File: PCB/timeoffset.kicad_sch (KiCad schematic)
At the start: 10 parts, among them J1 Conn_01x03, Q1 IRF7204_jandevalua, U1 ATtiny13A-SU

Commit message: Smaller form
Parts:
- added J2: Conn_01x03, Connector_JST:JST_PH_S3B-PH-K_1x03_P2.00mm_Horizontal, symbol Connector_Generic:Conn_01x03
- D1: footprint Diode_SMD:D_SMB -> Diode_SMD:D_SMA
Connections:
- net at C1.1, C2.1, D1.1 (K)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: now also J2.2 (Pin_2); no longer Q1.1 (S2), R2.2
- net at D1.2 (A), J1.2 (Pin_2), R1.1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: now also J2.1 (Pin_1)
- new net: J2.3 (Pin_3), Q1.1 (S2), R2.2
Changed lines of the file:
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@@
-(kicad_sch (version 20201015) (generator eeschema)
-  (page 1 1)
+(kicad_sch (version 20210621) (generator eeschema)
   (paper "A4")
-  (junction (at 64.77 46.99) (diameter 1.016) (color 0 0 0 0))
+  (junction (at 64.77 40.64) (diameter 1.016) (color 0 0 0 0))
   (junction (at 71.12 52.07) (diameter 1.016) (color 0 0 0 0))
   (junction (at 71.12 87.63) (diameter 1.016) (color 0 0 0 0))
   (junction (at 77.47 52.07) (diameter 1.016) (color 0 0 0 0))
   (junction (at 77.47 87.63) (diameter 1.016) (color 0 0 0 0))
+  (junction (at 88.8615 40.64) (diameter 1.016) (color 0 0 0 0))
   (junction (at 88.9 40.64) (diameter 1.016) (color 0 0 0 0))
   (junction (at 99.06 87.63) (diameter 1.016) (color 0 0 0 0))
-  (junction (at 99.06 91.44) (diameter 1.016) (color 0 0 0 0))
   (junction (at 119.38 60.96) (diameter 1.016) (color 0 0 0 0))
   (junction (at 119.38 74.93) (diameter 1.016) (color 0 0 0 0))
   (junction (at 119.38 87.63) (diameter 1.016) (color 0 0 0 0))
-  (junction (at 121.92 46.99) (diameter 1.016) (color 0 0 0 0))
+  (junction (at 121.92 46.9746) (diameter 1.016) (color 0 0 0 0))
   (junction (at 132.08 38.1) (diameter 1.016) (color 0 0 0 0))
   (wire (pts (xy 58.42 33.02) (xy 58.42 87.63))
@@
     (stroke (width 0) (type solid) (color 0 0 0 0))
   )
-  (wire (pts (xy 64.77 40.64) (xy 64.77 46.99))
-    (stroke (width 0) (type solid) (color 0 0 0 0))
-  )
-  (wire (pts (xy 64.77 46.99) (xy 64.77 52.07))
-    (stroke (width 0) (type solid) (color 0 0 0 0))
-  )
-  (wire (pts (xy 64.77 46.99) (xy 121.92 46.99))
+  (wire (pts (xy 64.77 40.64) (xy 64.77 52.07))
     (stroke (width 0) (type solid) (color 0 0 0 0))
   )
@@
     (stroke (width 0) (type solid) (color 0 0 0 0))
   )
+  (wire (pts (xy 88.8615 40.64) (xy 83.185 40.64))
+    (stroke (width 0) (type solid) (color 0 0 0 0))
+  )
   (wire (pts (xy 88.9 33.02) (xy 88.9 40.64))
     (stroke (width 0) (type solid) (color 0 0 0 0))
   )
-  (wire (pts (xy 88.9 40.64) (xy 83.185 40.64))
+  (wire (pts (xy 88.9 40.64) (xy 88.8615 40.64))
+    (stroke (width 0) (type solid) (color 0 0 0 0))
+  )
+  (wire (pts (xy 89.4385 43.5642) (xy 88.8615 40.64))
+    (stroke (width 0) (type solid) (color 0 0 0 0))
+  )
+  (wire (pts (xy 89.4385 46.1042) (xy 64.77 40.64))
+    (stroke (width 0) (type solid) (color 0 0 0 0))
+  )
+  (wire (pts (xy 89.4385 48.6442) (xy 121.92 46.9746))
     (stroke (width 0) (type solid) (color 0 0 0 0))
   )
@@
     (stroke (width 0) (type solid) (color 0 0 0 0))
   )
-  (wire (pts (xy 99.06 87.63) (xy 99.06 91.44))
-    (stroke (width 0) (type solid) (color 0 0 0 0))
-  )
-  (wire (pts (xy 99.06 91.44) (xy 99.06 92.71))
+  (wire (pts (xy 99.06 87.63) (xy 99.06 92.71))
+    (stroke (width 0) (type solid) (color 0 0 0 0))
+  )
+  (wire (pts (xy 99.06 92.71) (xy 99.0762 92.9399))
     (stroke (width 0) (type solid) (color 0 0 0 0))
   )
@@
     (stroke (width 0) (type solid) (color 0 0 0 0))
   )
-  (wire (pts (xy 121.92 45.72) (xy 121.92 46.99))
+  (wire (pts (xy 121.92 45.72) (xy 121.92 46.9746))
+    (stroke (width 0) (type solid) (color 0 0 0 0))
+  )
+  (wire (pts (xy 121.92 46.9746) (xy 121.92 46.99))
     (stroke (width 0) (type solid) (color 0 0 0 0))
   )
@@
     (stroke (width 0) (type solid) (color 0 0 0 0))
   )
-  (symbol (lib_id "power:GND") (at 99.06 91.44 0) (unit 1)
-    (in_bom yes) (on_board yes)
-    (property "Reference" "#PWR0101" (id 0) (at 99.06 97.79 0)
-      (effects (font (size 1.27 1.27)) hide)
-    )
-    (property "Value" "GND" (id 1) (at 99.187 95.8342 0))
-    (property "Footprint" "" (id 2) (at 99.06 91.44 0)
-      (effects (font (size 1.27 1.27)) hide)
-    )
-    (property "Datasheet" "" (id 3) (at 99.06 91.44 0)
-      (effects (font (size 1.27 1.27)) hide)
-    )
+  (symbol (lib_id "power:GND") (at 99.0762 92.9399 0) (unit 1)
+    (in_bom yes) (on_board yes)
+    (property "Reference" "#PWR01" (id 0) (at 99.0762 99.2899 0)
+      (effects (font (size 1.27 1.27)) hide)
+    )
+    (property "Value" "GND" (id 1) (at 99.2032 97.3341 0))
+    (property "Footprint" "" (id 2) (at 99.0762 92.9399 0)
+      (effects (font (size 1.27 1.27)) hide)
+    )
+    (property "Datasheet" "" (id 3) (at 99.0762 92.9399 0)
+      (effects (font (size 1.27 1.27)) hide)
+    )
+    (pin "1")
   )
   (symbol (lib_id "Device:R_Small") (at 119.38 72.39 0) (unit 1)
@@
       (effects (font (size 1.27 1.27)) hide)
     )
+    (pin "1")
+    (pin "2")
   )
   (symbol (lib_id "Device:R_Small") (at 121.92 43.18 0) (unit 1)
@@
       (effects (font (size 1.27 1.27)) hide)
     )
+    (pin "1")
+    (pin "2")
   )
   (symbol (lib_id "timeoffset-rescue:CP_Small-Device") (at 71.12 67.31 0) (unit 1)
@@
       (effects (font (size 1.27 1.27)) hide)
     )
+    (pin "1")
+    (pin "2")
   )
   (symbol (lib_id "Device:C_Small") (at 77.47 67.31 0) (unit 1)
@@
       (effects (font (size 1.27 1.27)) hide)
     )
+    (pin "1")
+    (pin "2")
   )
   (symbol (lib_id "Device:C_Small") (at 119.38 81.915 0) (unit 1)
@@
       (effects (font (size 1.27 1.27)) hide)
     )
+    (pin "1")
+    (pin "2")
   )
   (symbol (lib_id "Device:D") (at 79.375 40.64 0) (unit 1)
@@
     (property "Reference" "D1" (id 0) (at 79.375 35.1536 0))
     (property "Value" "D" (id 1) (at 79.375 37.465 0))
-    (property "Footprint" "Diode_SMD:D_SMB" (id 2) (at 79.375 40.64 0)
+    (property "Footprint" "Diode_SMD:D_SMA" (id 2) (at 79.375 40.64 0)
       (effects (font (size 1.27 1.27)) hide)
     )
@@
       (effects (font (size 1.27 1.27)) hide)
     )
+    (pin "1")
+    (pin "2")
   )
   (symbol (lib_id "Connector_Generic:Conn_01x03") (at 88.9 27.94 90) (unit 1)
@@
       (effects (font (size 1.27 1.27)) hide)
     )
+    (pin "1")
+    (pin "2")
+    (pin "3")
+  )
+  (symbol (lib_id "Connector_Generic:Conn_01x03") (at 94.5185 46.1042 0) (unit 1)
+    (in_bom yes) (on_board yes)
+    (property "Reference" "J2" (id 0) (at 96.5506 45.0056 0)
+      (effects (font (size 1.27 1.27)) (justify left))
+    )
+    (property "Value" "Conn_01x03" (id 1) (at 96.5506 47.3043 0)
+      (effects (font (size 1.27 1.27)) (justify left))
+    )
+    (property "Footprint" "Connector_JST:JST_PH_S3B-PH-K_1x03_P2.00mm_Horizontal" (id 2) (at 94.5185 46.1042 0)
+      (effects (font (size 1.27 1.27)) hide)
+    )
+    (property "Datasheet" "~" (id 3) (at 94.5185 46.1042 0)
+      (effects (font (size 1.27 1.27)) hide)
+    )
+    (pin "1")
+    (pin "2")
+    (pin "3")
   )
   (symbol (lib_id "timeoffset-rescue:IRF7204_jandevalua-7204") (at 132.08 44.45 270) (unit 2)
@@
       (effects (font (size 1.27 1.27)) (justify left) hide)
     )
+    (pin "1")
+    (pin "2")
+    (pin "3")
   )
   (symbol (lib_id "Connector_Generic:Conn_02x03_Odd_Even") (at 143.51 68.58 0) (unit 1)
@@
       (effects (font (size 1.27 1.27)) hide)
     )
+    (pin "1")
+    (pin "2")
+    (pin "3")
+    (pin "4")
+    (pin "5")
+    (pin "6")
   )
   (symbol (lib_id "timeoffset-rescue:ATtiny13A-SU-MCU_Microchip_ATtiny") (at 99.06 69.85 0) (unit 1)
@@
       (effects (font (size 1.27 1.27)) hide)
     )
+    (pin "1")
+    (pin "2")
+    (pin "3")
+    (pin "4")
+    (pin "5")
+    (pin "6")
+    (pin "7")
+    (pin "8")
   )
   (sheet_instances
@@
   (symbol_instances
     (path "/00000000-0000-0000-0000-00005ddfc2da"
-      (reference "#PWR0101") (unit 1) (value "GND") (footprint "")
+      (reference "#PWR01") (unit 1) (value "GND") (footprint "")
     )
     (path "/00000000-0000-0000-0000-00005ddfc5f2"
@@
     )
     (path "/00000000-0000-0000-0000-00005e2e145b"
-      (reference "D1") (unit 1) (value "D") (footprint "Diode_SMD:D_SMB")
+      (reference "D1") (unit 1) (value "D") (footprint "Diode_SMD:D_SMA")
     )
     (path "/00000000-0000-0000-0000-00005de06ca8"
       (reference "J1") (unit 1) (value "Conn_01x03") (footprint "Connector_PinHeader_2.54mm:PinHeader_1x03_P2.54mm_Vertical")
     )
+    (path "/33fe6c4e-0011-4e87-b903-abc10fce3756"
+      (reference "J2") (unit 1) (value "Conn_01x03") (footprint "Connector_JST:JST_PH_S3B-PH-K_1x03_P2.00mm_Horizontal")
+    )
     (path "/00000000-0000-0000-0000-00005de29fca"

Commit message: board optimization
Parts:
- removed J2: Conn_01x03, Connector_JST:JST_PH_S3B-PH-K_1x03_P2.00mm_Horizontal, symbol Connector_Generic:Conn_01x03
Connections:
- net at C1.1, C2.1, D1.1 (K)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: now also Q1.1 (S2), R2.2
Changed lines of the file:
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@@
 (kicad_sch (version 20210621) (generator eeschema)
   (paper "A4")
-  (junction (at 64.77 40.64) (diameter 1.016) (color 0 0 0 0))
+  (junction (at 64.77 46.961) (diameter 1.016) (color 0 0 0 0))
   (junction (at 71.12 52.07) (diameter 1.016) (color 0 0 0 0))
   (junction (at 71.12 87.63) (diameter 1.016) (color 0 0 0 0))
   (junction (at 77.47 52.07) (diameter 1.016) (color 0 0 0 0))
   (junction (at 77.47 87.63) (diameter 1.016) (color 0 0 0 0))
-  (junction (at 88.8615 40.64) (diameter 1.016) (color 0 0 0 0))
   (junction (at 88.9 40.64) (diameter 1.016) (color 0 0 0 0))
   (junction (at 99.06 87.63) (diameter 1.016) (color 0 0 0 0))
@@
   (junction (at 119.38 74.93) (diameter 1.016) (color 0 0 0 0))
   (junction (at 119.38 87.63) (diameter 1.016) (color 0 0 0 0))
-  (junction (at 121.92 46.9746) (diameter 1.016) (color 0 0 0 0))
+  (junction (at 121.92 46.99) (diameter 1.016) (color 0 0 0 0))
   (junction (at 132.08 38.1) (diameter 1.016) (color 0 0 0 0))
   (wire (pts (xy 58.42 33.02) (xy 58.42 87.63))
@@
     (stroke (width 0) (type solid) (color 0 0 0 0))
   )
-  (wire (pts (xy 64.77 40.64) (xy 64.77 52.07))
+  (wire (pts (xy 64.77 40.64) (xy 64.77 46.961))
+    (stroke (width 0) (type solid) (color 0 0 0 0))
+  )
+  (wire (pts (xy 64.77 46.961) (xy 64.77 52.07))
     (stroke (width 0) (type solid) (color 0 0 0 0))
   )
@@
     (stroke (width 0) (type solid) (color 0 0 0 0))
   )
-  (wire (pts (xy 88.8615 40.64) (xy 83.185 40.64))
+  (wire (pts (xy 83.185 40.64) (xy 88.9 40.64))
     (stroke (width 0) (type solid) (color 0 0 0 0))
   )
@@
     (stroke (width 0) (type solid) (color 0 0 0 0))
   )
-  (wire (pts (xy 88.9 40.64) (xy 88.8615 40.64))
-    (stroke (width 0) (type solid) (color 0 0 0 0))
-  )
-  (wire (pts (xy 89.4385 43.5642) (xy 88.8615 40.64))
-    (stroke (width 0) (type solid) (color 0 0 0 0))
-  )
-  (wire (pts (xy 89.4385 46.1042) (xy 64.77 40.64))
-    (stroke (width 0) (type solid) (color 0 0 0 0))
-  )
-  (wire (pts (xy 89.4385 48.6442) (xy 121.92 46.9746))
-    (stroke (width 0) (type solid) (color 0 0 0 0))
-  )
   (wire (pts (xy 99.06 52.07) (xy 77.47 52.07))
     (stroke (width 0) (type solid) (color 0 0 0 0))
@@
     (stroke (width 0) (type solid) (color 0 0 0 0))
   )
-  (wire (pts (xy 121.92 45.72) (xy 121.92 46.9746))
-    (stroke (width 0) (type solid) (color 0 0 0 0))
-  )
-  (wire (pts (xy 121.92 46.9746) (xy 121.92 46.99))
+  (wire (pts (xy 121.92 45.72) (xy 121.92 46.99))
+    (stroke (width 0) (type solid) (color 0 0 0 0))
+  )
+  (wire (pts (xy 121.92 46.99) (xy 64.77 46.961))
     (stroke (width 0) (type solid) (color 0 0 0 0))
   )
@@
     )
     (property "Datasheet" "~" (id 3) (at 88.9 27.94 0)
-      (effects (font (size 1.27 1.27)) hide)
-    )
-    (pin "1")
-    (pin "2")
-    (pin "3")
-  )
-  (symbol (lib_id "Connector_Generic:Conn_01x03") (at 94.5185 46.1042 0) (unit 1)
-    (in_bom yes) (on_board yes)
-    (property "Reference" "J2" (id 0) (at 96.5506 45.0056 0)
-      (effects (font (size 1.27 1.27)) (justify left))
-    )
-    (property "Value" "Conn_01x03" (id 1) (at 96.5506 47.3043 0)
-      (effects (font (size 1.27 1.27)) (justify left))
-    )
-    (property "Footprint" "Connector_JST:JST_PH_S3B-PH-K_1x03_P2.00mm_Horizontal" (id 2) (at 94.5185 46.1042 0)
-      (effects (font (size 1.27 1.27)) hide)
-    )
-    (property "Datasheet" "~" (id 3) (at 94.5185 46.1042 0)
       (effects (font (size 1.27 1.27)) hide)
     )
@@
       (reference "J1") (unit 1) (value "Conn_01x03") (footprint "Connector_PinHeader_2.54mm:PinHeader_1x03_P2.54mm_Vertical")
     )
-    (path "/33fe6c4e-0011-4e87-b903-abc10fce3756"
-      (reference "J2") (unit 1) (value "Conn_01x03") (footprint "Connector_JST:JST_PH_S3B-PH-K_1x03_P2.00mm_Horizontal")
-    )
     (path "/00000000-0000-0000-0000-00005de29fca"

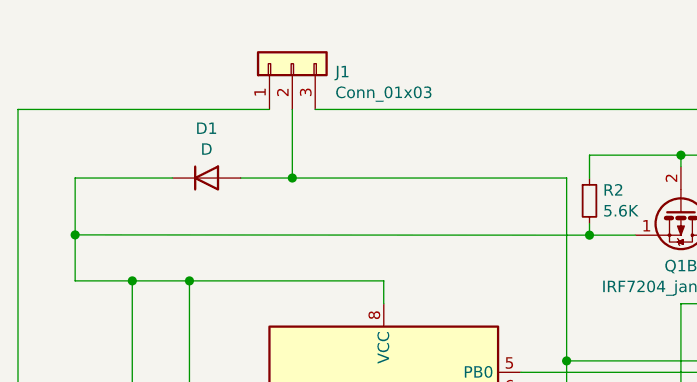
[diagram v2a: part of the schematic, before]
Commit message: horizontal connectors added
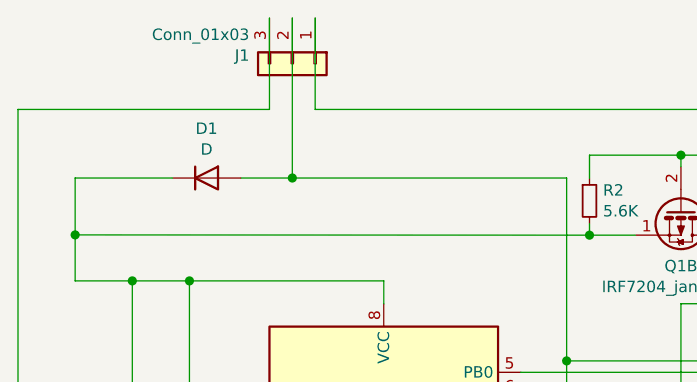
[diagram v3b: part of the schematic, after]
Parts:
- J1: footprint Connector_PinHeader_2.54mm:PinHeader_1x03_P2.54mm_Vertical -> Connector_JST:JST_PH_S3B-PH-K_1x03_P2.00mm_Horizontal
- SPI_In1: footprint Connector_PinHeader_2.54mm:PinHeader_2x03_P2.54mm_Vertical -> Connector_PinHeader_2.54mm:PinHeader_2x03_P2.54mm_Horizontal
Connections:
- net GND: now also J1.3 (Pin_3); no longer J1.1 (Pin_1)
- net at Q1.3 (D2): now also J1.1 (Pin_1); no longer J1.3 (Pin_3)
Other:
- moved on the sheet: J1
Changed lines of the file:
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@@
     (stroke (width 0) (type solid) (color 0 0 0 0))
   )
-  (wire (pts (xy 88.9 33.02) (xy 88.9 40.64))
+  (wire (pts (xy 86.36 22.86) (xy 86.36 33.02))
+    (stroke (width 0) (type solid) (color 0 0 0 0))
+  )
+  (wire (pts (xy 88.9 22.86) (xy 88.9 40.64))
+    (stroke (width 0) (type solid) (color 0 0 0 0))
+  )
+  (wire (pts (xy 91.44 22.86) (xy 91.44 33.02))
     (stroke (width 0) (type solid) (color 0 0 0 0))
   )
@@
     (pin "2")
   )
-  (symbol (lib_id "Connector_Generic:Conn_01x03") (at 88.9 27.94 90) (unit 1)
-    (in_bom yes) (on_board yes)
-    (property "Reference" "J1" (id 0) (at 93.6752 28.8544 90)
+  (symbol (lib_id "Connector_Generic:Conn_01x03") (at 88.9 27.94 270) (unit 1)
+    (in_bom yes) (on_board yes)
+    (property "Reference" "J1" (id 0) (at 84.1248 27.0256 90)
       (effects (font (size 1.27 1.27)) (justify right))
     )
-    (property "Value" "Conn_01x03" (id 1) (at 93.6752 31.1658 90)
+    (property "Value" "Conn_01x03" (id 1) (at 84.1248 24.7142 90)
       (effects (font (size 1.27 1.27)) (justify right))
     )
-    (property "Footprint" "Connector_PinHeader_2.54mm:PinHeader_1x03_P2.54mm_Vertical" (id 2) (at 88.9 27.94 0)
+    (property "Footprint" "Connector_JST:JST_PH_S3B-PH-K_1x03_P2.00mm_Horizontal" (id 2) (at 88.9 27.94 0)
       (effects (font (size 1.27 1.27)) hide)
     )
@@
     (property "Reference" "SPI_In1" (id 0) (at 144.78 60.5282 0))
     (property "Value" "Conn_02x03_Odd_Even" (id 1) (at 144.78 62.8396 0))
-    (property "Footprint" "Connector_PinHeader_2.54mm:PinHeader_2x03_P2.54mm_Vertical" (id 2) (at 143.51 68.58 0)
+    (property "Footprint" "Connector_PinHeader_2.54mm:PinHeader_2x03_P2.54mm_Horizontal" (id 2) (at 143.51 68.58 0)
       (effects (font (size 1.27 1.27)) hide)
     )
@@
     )
     (path "/00000000-0000-0000-0000-00005de06ca8"
-      (reference "J1") (unit 1) (value "Conn_01x03") (footprint "Connector_PinHeader_2.54mm:PinHeader_1x03_P2.54mm_Vertical")
+      (reference "J1") (unit 1) (value "Conn_01x03") (footprint "Connector_JST:JST_PH_S3B-PH-K_1x03_P2.00mm_Horizontal")
     )
     (path "/00000000-0000-0000-0000-00005de29fca"
@@
     )
     (path "/00000000-0000-0000-0000-00005de00932"
-      (reference "SPI_In1") (unit 1) (value "Conn_02x03_Odd_Even") (footprint "Connector_PinHeader_2.54mm:PinHeader_2x03_P2.54mm_Vertical")
+      (reference "SPI_In1") (unit 1) (value "Conn_02x03_Odd_Even") (footprint "Connector_PinHeader_2.54mm:PinHeader_2x03_P2.54mm_Horizontal")
     )
     (path "/00000000-0000-0000-0000-00005ddfc2a1"

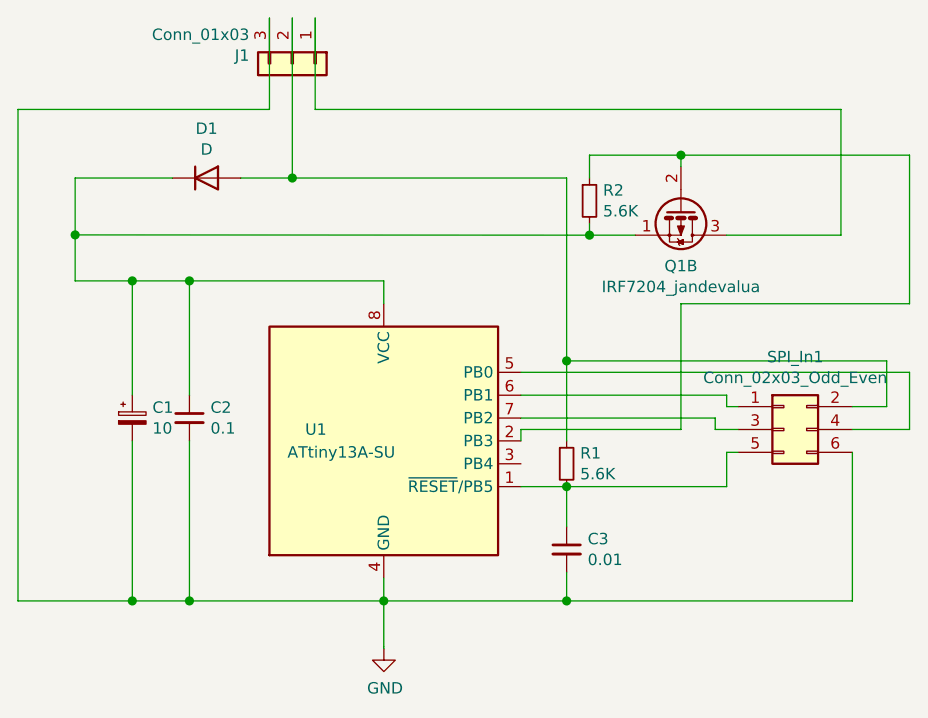
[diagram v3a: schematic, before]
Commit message: Reset fix
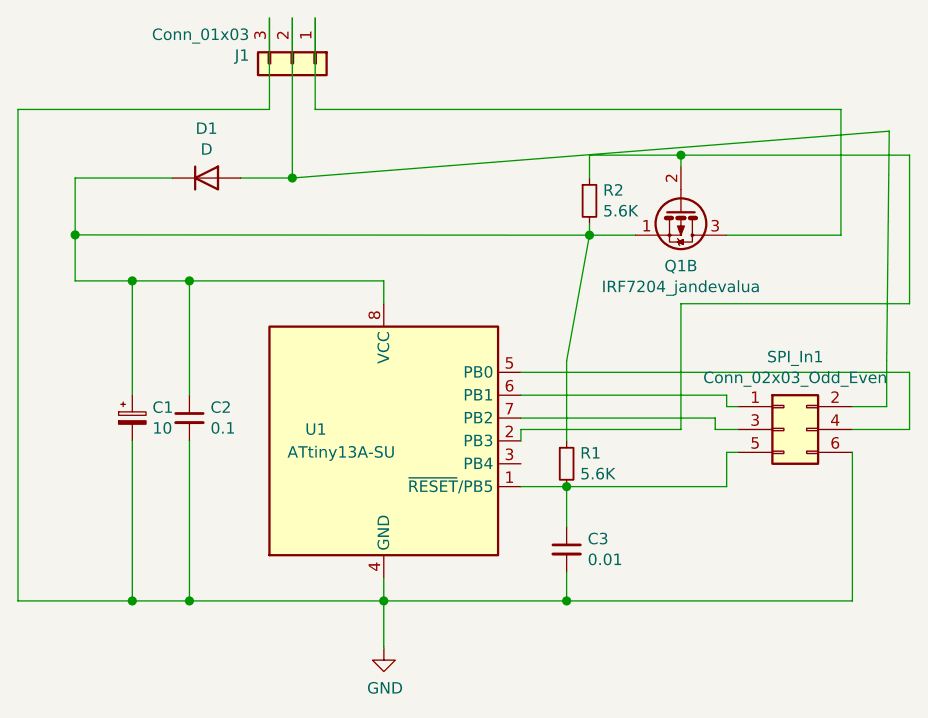
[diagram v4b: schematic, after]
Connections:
- net at C1.1, C2.1, D1.1 (K)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: now also R1.1
- net at D1.2 (A), J1.2 (Pin_2), SPI_In1.2 (Pin_2): no longer R1.1
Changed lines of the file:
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@@
   (junction (at 88.9 40.64) (diameter 1.016) (color 0 0 0 0))
   (junction (at 99.06 87.63) (diameter 1.016) (color 0 0 0 0))
-  (junction (at 119.38 60.96) (diameter 1.016) (color 0 0 0 0))
   (junction (at 119.38 74.93) (diameter 1.016) (color 0 0 0 0))
   (junction (at 119.38 87.63) (diameter 1.016) (color 0 0 0 0))
@@
     (stroke (width 0) (type solid) (color 0 0 0 0))
   )
-  (wire (pts (xy 119.38 40.64) (xy 88.9 40.64))
-    (stroke (width 0) (type solid) (color 0 0 0 0))
-  )
-  (wire (pts (xy 119.38 40.64) (xy 119.38 60.96))
-    (stroke (width 0) (type solid) (color 0 0 0 0))
-  )
   (wire (pts (xy 119.38 60.96) (xy 119.38 69.85))
-    (stroke (width 0) (type solid) (color 0 0 0 0))
-  )
-  (wire (pts (xy 119.38 60.96) (xy 154.94 60.96))
     (stroke (width 0) (type solid) (color 0 0 0 0))
   )
@@
   )
   (wire (pts (xy 121.92 46.99) (xy 64.77 46.961))
+    (stroke (width 0) (type solid) (color 0 0 0 0))
+  )
+  (wire (pts (xy 121.92 46.99) (xy 119.38 60.96))
     (stroke (width 0) (type solid) (color 0 0 0 0))
   )
@@
     (stroke (width 0) (type solid) (color 0 0 0 0))
   )
+  (wire (pts (xy 154.94 60.96) (xy 155.2264 35.4342))
+    (stroke (width 0) (type solid) (color 0 0 0 0))
+  )
   (wire (pts (xy 154.94 66.04) (xy 151.13 66.04))
     (stroke (width 0) (type solid) (color 0 0 0 0))
   )
+  (wire (pts (xy 155.2264 35.4342) (xy 88.9 40.64))
+    (stroke (width 0) (type solid) (color 0 0 0 0))
+  )
